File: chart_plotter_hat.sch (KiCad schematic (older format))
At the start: 45 parts, among them J1 JST PH, J2 JST PH, J3 40HAT, J4 JST PH, J5 JST PH, J6 JST PH, J7 JST PH, J8 Conn_02x03_Odd_Even, J9 JST PH, Q1 DMG2305UX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

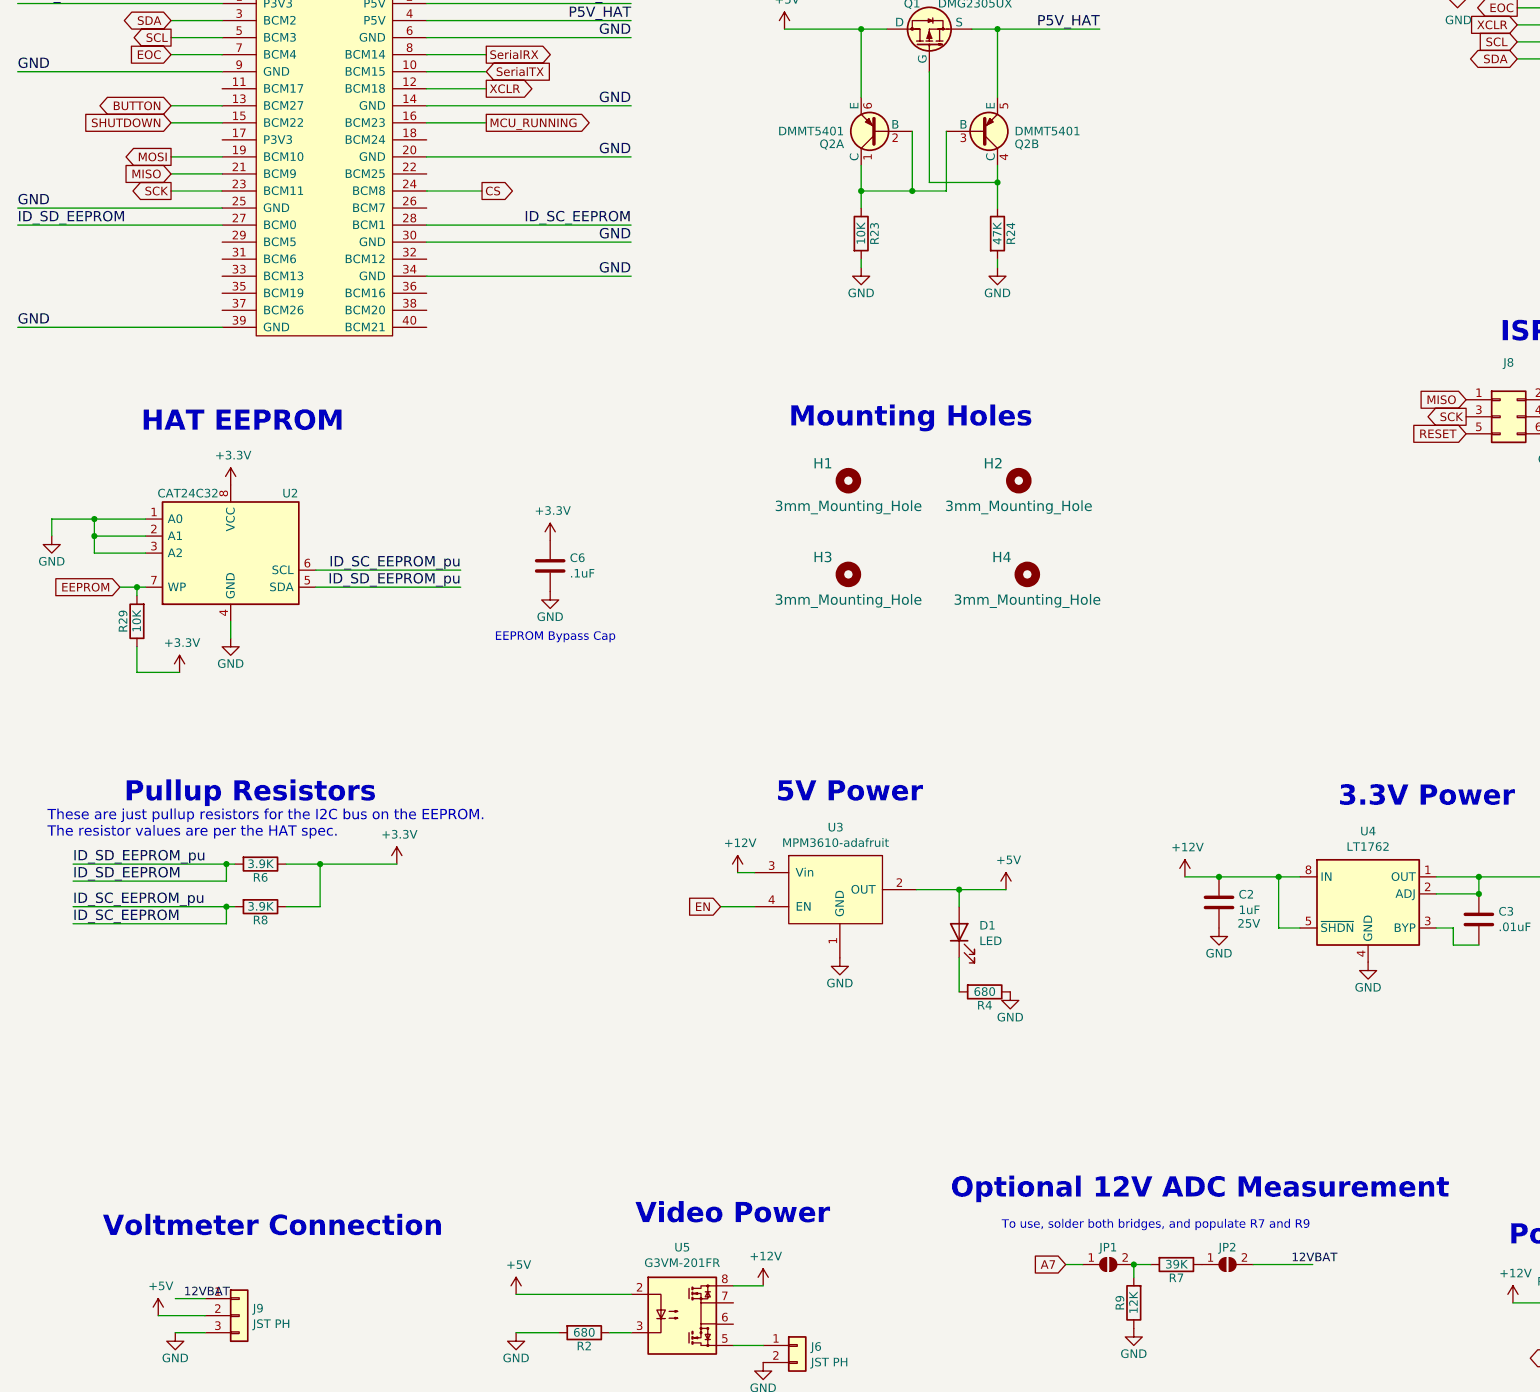
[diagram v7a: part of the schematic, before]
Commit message: Removed Jumper2, don't need
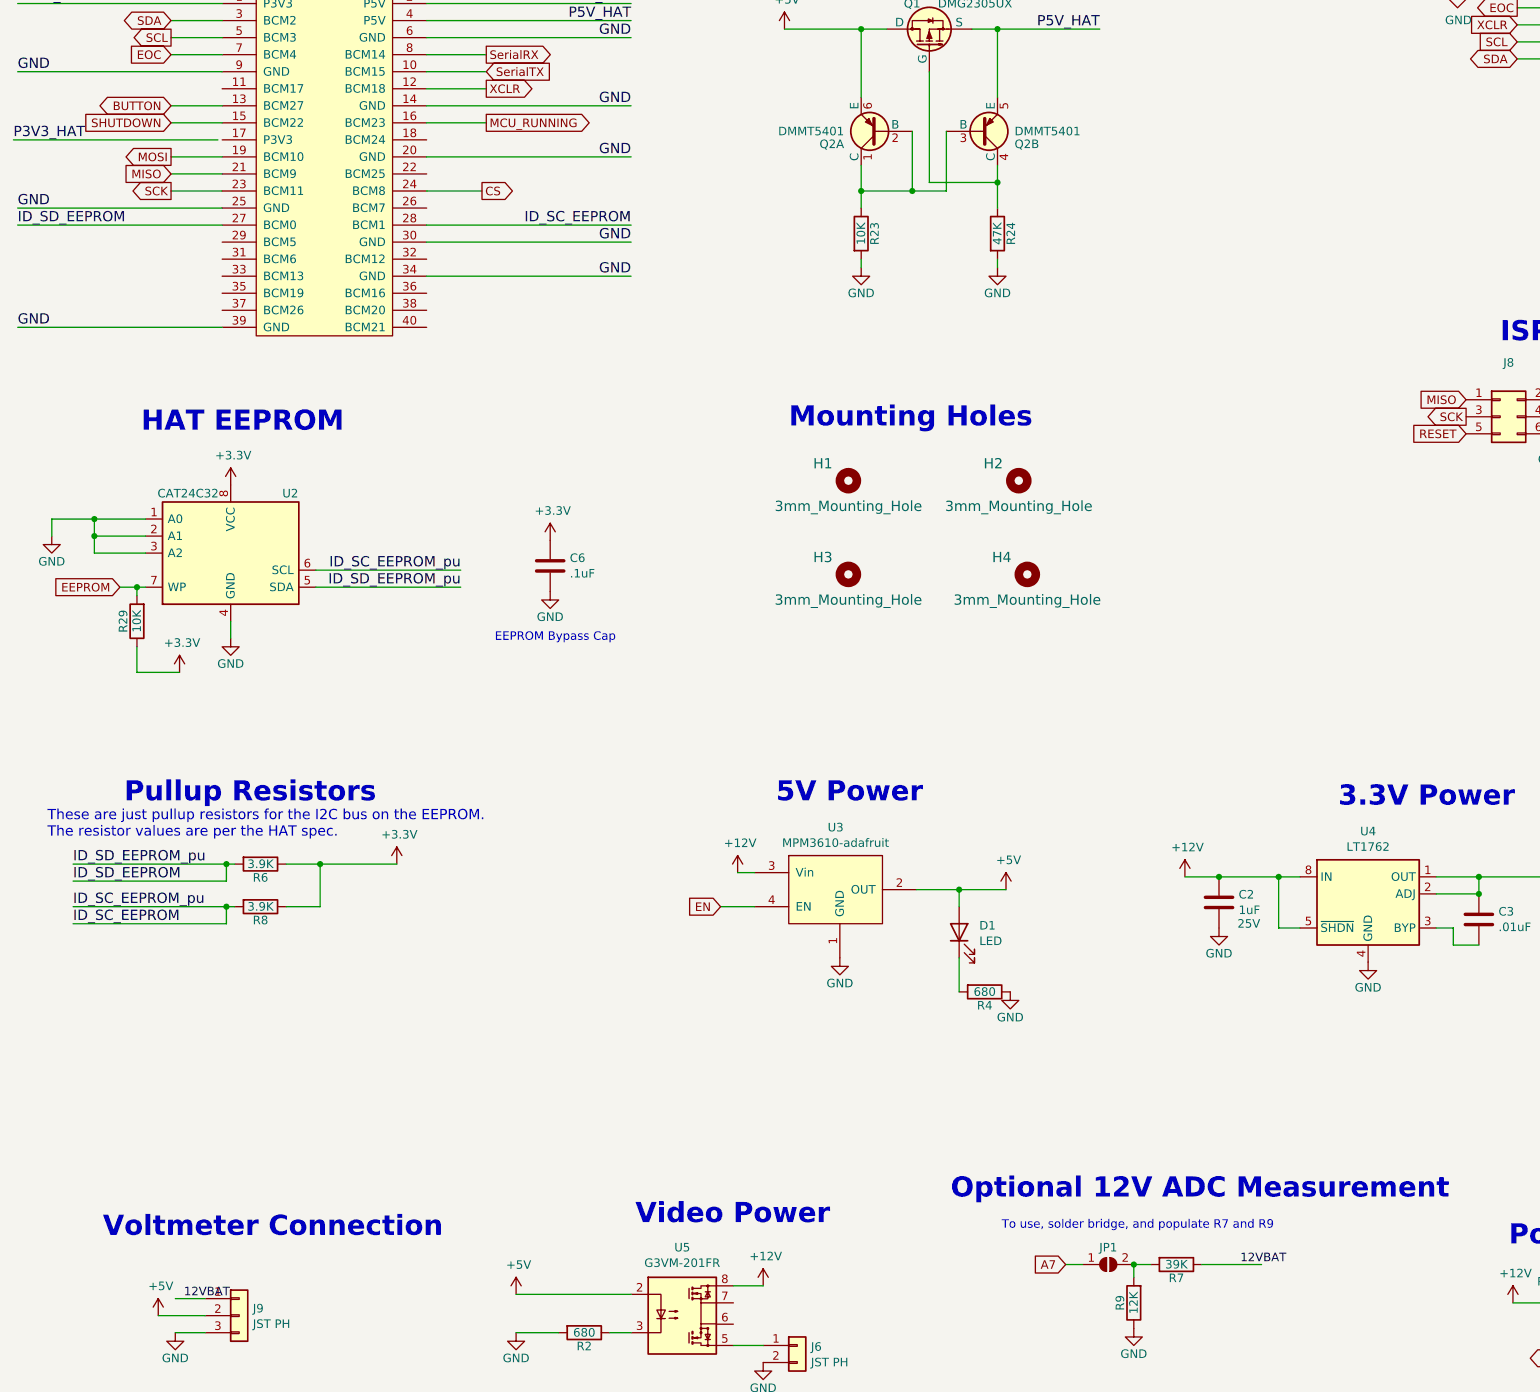
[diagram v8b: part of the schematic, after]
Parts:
- removed JP2: SolderJumper_2_Open, CustomComponents:SolderJumper-2_P1.3mm_Open_RoundedPad1.0x1.5mm, symbol Jumper:SolderJumper_2_Open
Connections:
- net 12VBAT: now also R7.1
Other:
- note added: "To use, solder bridge, and populate R7 and R9"
- note removed: "To use, solder both bridges, and populate R7 and R9"
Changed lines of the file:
@@
 Wire Wire Line
 	6950 9650 7050 9650
-$Comp
-L Jumper:SolderJumper_2_Open JP2
-U 1 1 6002B929
-P 7900 9650
-F 0 "JP2" H 7900 9750 50  0000 C CNN
-F 1 "SolderJumper_2_Open" H 7900 9764 50  0001 C CNN
-F 2 "CustomComponents:SolderJumper-2_P1.3mm_Open_RoundedPad1.0x1.5mm" H 7900 9650 50  0001 C CNN
-F 3 "~" H 7900 9650 50  0001 C CNN
-	1    7900 9650
-	1    0    0    -1
-$EndComp
 Wire Wire Line
-	8050 9650 8400 9650
-Text Label 8275 9650 0    50   ~ 0
+	7750 9650 8100 9650
+Text Label 7975 9650 0    50   ~ 0
 12VBAT
 Text Notes 6275 9275 0    118  ~ 24
@@
 $EndComp
 Text Notes 6575 9450 0    50   ~ 0
-To use, solder both bridges, and populate R7 and R9
+To use, solder bridge, and populate R7 and R9
 Wire Wire Line
 	13100 6025 13375 6025
@@
 Wire Wire Line
 	1700 2850 2000 2850
+Text Label 775  3050 0    60   ~ 0
+P3V3_HAT
+Wire Wire Line
+	1975 3050 775  3050
 $EndSCHEMATC
